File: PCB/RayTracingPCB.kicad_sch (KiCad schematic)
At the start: 1 part, among them J1 Conn_ARM_JTAG_SWD_10

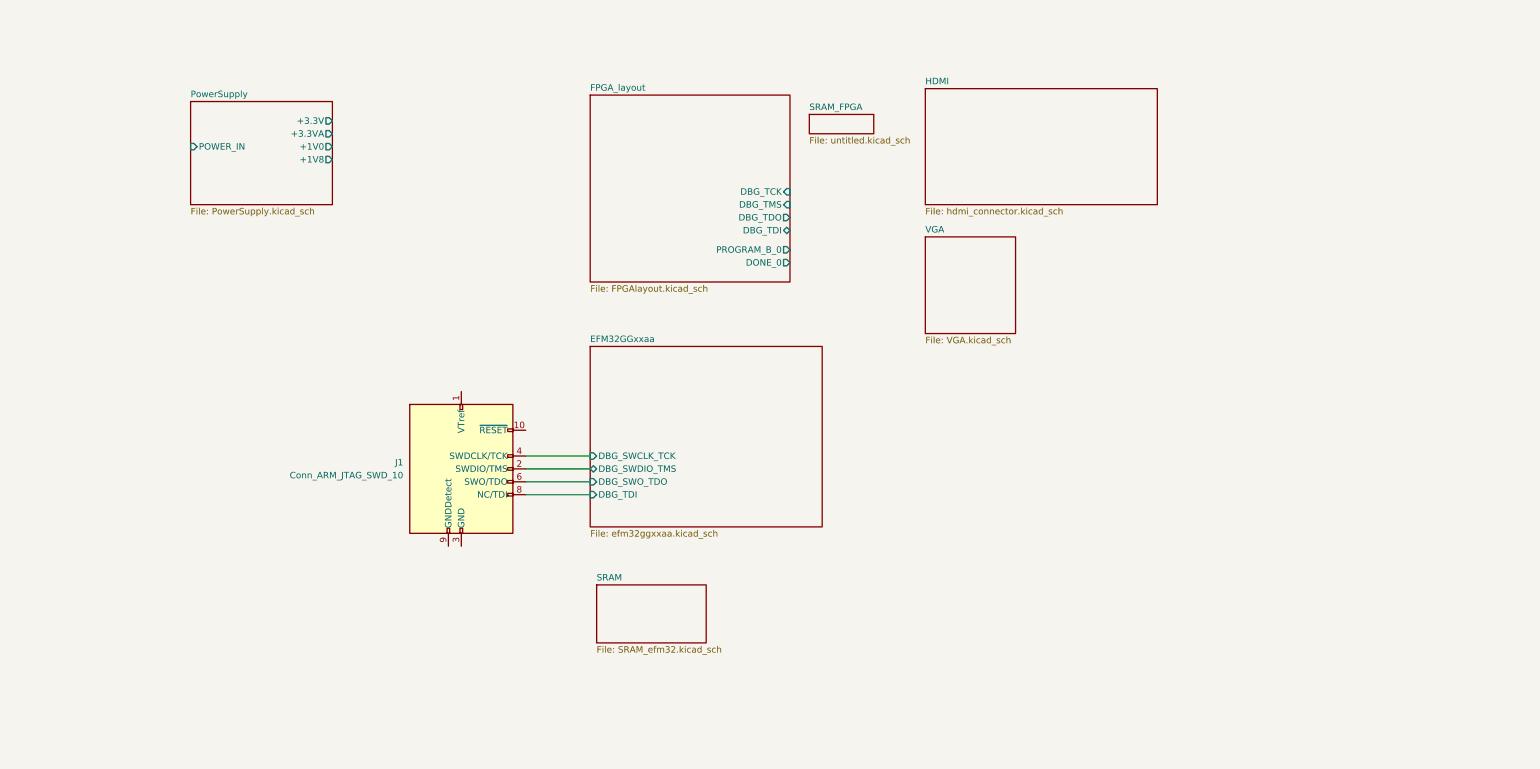
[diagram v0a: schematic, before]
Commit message: Trace QSPI for MCU Master (#7), slaves unconnected
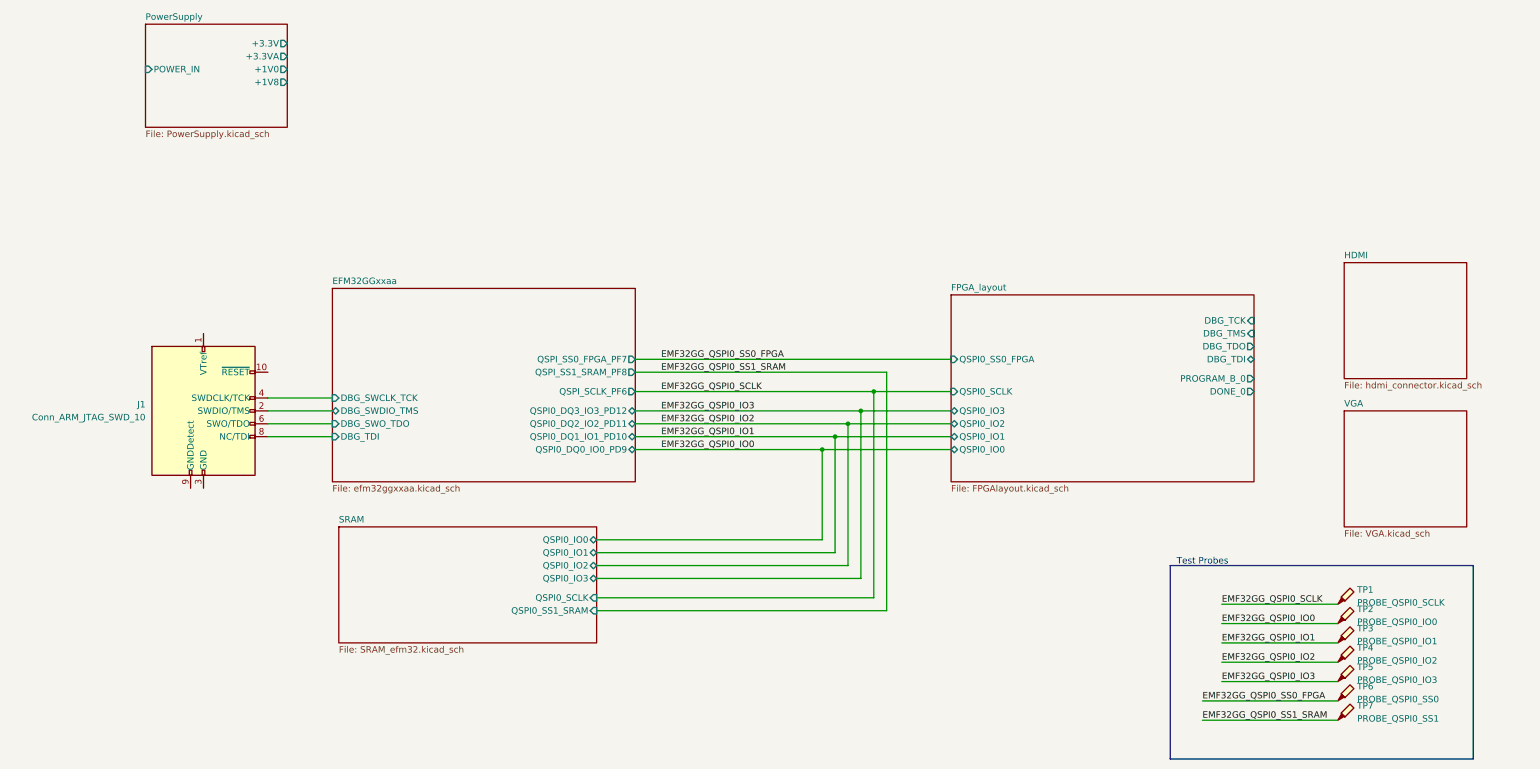
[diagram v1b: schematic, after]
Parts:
- added TP1: PROBE_QSPI0_SCLK, symbol Connector:TestPoint_Probe
- added TP2: PROBE_QSPI0_IO0, symbol Connector:TestPoint_Probe
- added TP3: PROBE_QSPI0_IO1, symbol Connector:TestPoint_Probe
- added TP4: PROBE_QSPI0_IO2, symbol Connector:TestPoint_Probe
- added TP5: PROBE_QSPI0_IO3, symbol Connector:TestPoint_Probe
- added TP6: PROBE_QSPI0_SS0, symbol Connector:TestPoint_Probe
- added TP7: PROBE_QSPI0_SS1, symbol Connector:TestPoint_Probe
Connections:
- new net EMF32GG_QSPI0_IO0: TP2.1
- new net EMF32GG_QSPI0_IO1: TP3.1
- new net EMF32GG_QSPI0_IO2: TP4.1
- new net EMF32GG_QSPI0_IO3: TP5.1
- new net EMF32GG_QSPI0_SCLK: TP1.1
- new net EMF32GG_QSPI0_SS0_FPGA: TP6.1
- new net EMF32GG_QSPI0_SS1_SRAM: TP7.1
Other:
- removed sheet SRAM_FPGA
- sheet EFM32GGxxaa ports: added QSPI0_DQ0_IO0_PD9, QSPI0_DQ1_IO1_PD10, QSPI0_DQ2_IO2_PD11, QSPI0_DQ3_IO3_PD12, QSPI_SCLK_PF6, QSPI_SS0_FPGA_PF7, QSPI_SS1_SRAM_PF8; removed none
- sheet FPGA_layout ports: added QSPI0_IO0, QSPI0_IO1, QSPI0_IO2, QSPI0_IO3, QSPI0_SCLK, QSPI0_SS0_FPGA; removed none
- sheet SRAM ports: added QSPI0_IO0, QSPI0_IO1, QSPI0_IO2, QSPI0_IO3, QSPI0_SCLK, QSPI0_SS1_SRAM; removed none
- note added: "Test Probes"
- moved on the sheet: J1
